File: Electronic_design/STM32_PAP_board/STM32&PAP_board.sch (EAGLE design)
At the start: 22 parts

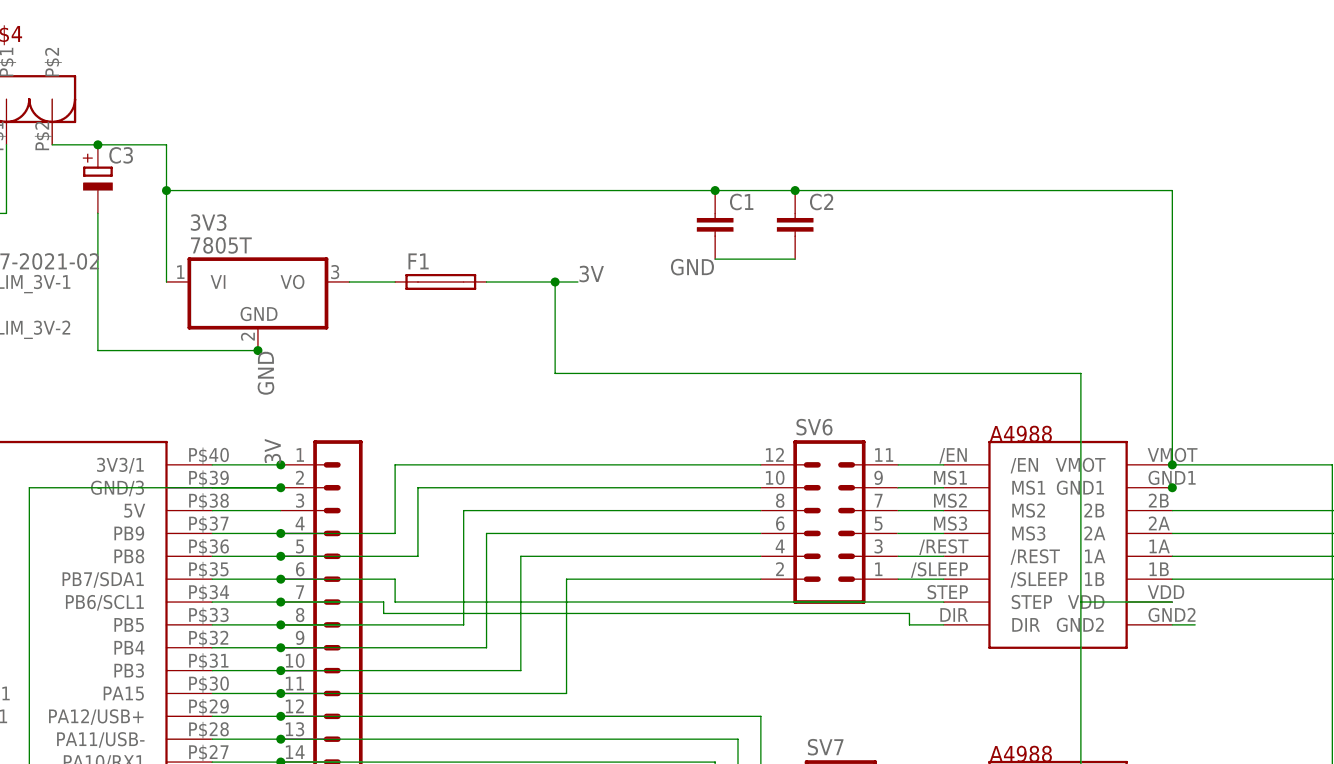
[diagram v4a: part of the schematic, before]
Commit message: modif sens connecteurs puissance
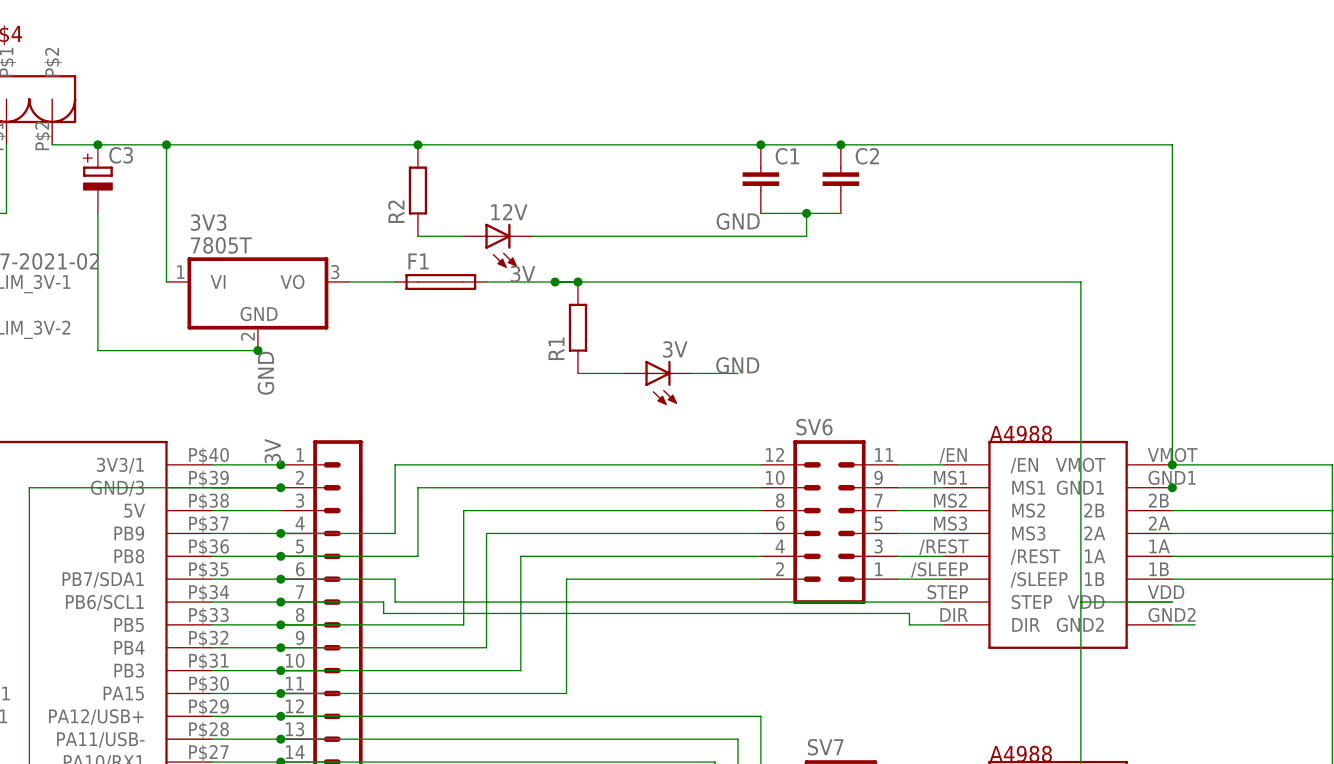
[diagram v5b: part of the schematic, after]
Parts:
- added 12V, 3V: (no value), eagle-ltspice:LED_ELD260
- added R1, R2: (no value), eagle-ltspice:R0204/7
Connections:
- new net N$43: 3V.A, R1.1
- new net N$47: 12V.A, R2.1
- net 3V: now also R1.2
- net GND: now also 12V.C, 3V.C
- net N$42: now also R2.2
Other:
- moved on the sheet: C1, C2
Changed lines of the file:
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@@
 <part name="SV2" library="con-lstb" library_urn="urn:adsk.eagle:library:162" deviceset="MA08-1" device="" package3d_urn="urn:adsk.eagle:package:8343/1"/>
 <part name="C3" library="rcl" library_urn="urn:adsk.eagle:library:334" deviceset="CPOL-EU" device="E5-13" package3d_urn="urn:adsk.eagle:package:23375/1"/>
+<part name="R1" library="eagle-ltspice" library_urn="urn:adsk.eagle:library:217" deviceset="R" device="0204/7" package3d_urn="urn:adsk.eagle:package:13274/1"/>
+<part name="3V" library="eagle-ltspice" library_urn="urn:adsk.eagle:library:217" deviceset="LED_E" device="LD260" package3d_urn="urn:adsk.eagle:package:13313/1"/>
+<part name="R2" library="eagle-ltspice" library_urn="urn:adsk.eagle:library:217" deviceset="R" device="0204/7" package3d_urn="urn:adsk.eagle:package:13274/1"/>
+<part name="12V" library="eagle-ltspice" library_urn="urn:adsk.eagle:library:217" deviceset="LED_E" device="LD260" package3d_urn="urn:adsk.eagle:package:13313/1"/>
 </parts>
 <sheets>
@@
 <instance part="SV10" gate="G$1" x="-106.68" y="-53.34"/>
 <instance part="SV11" gate="G$1" x="-125.73" y="-54.61"/>
-<instance part="C1" gate="G$1" x="35.56" y="58.42"/>
-<instance part="C2" gate="G$1" x="44.45" y="58.42"/>
+<instance part="C1" gate="G$1" x="40.64" y="63.5"/>
+<instance part="C2" gate="G$1" x="49.53" y="63.5"/>
 <instance part="F1" gate="1" x="5.08" y="50.8"/>
 <instance part="UART2" gate="G$1" x="-106.68" y="15.24"/>
@@
 <instance part="SV2" gate="1" x="-93.98" y="-5.08"/>
 <instance part="C3" gate="G$1" x="-33.02" y="63.5"/>
+<instance part="R1" gate="G$1" x="20.32" y="45.72" rot="R90"/>
+<instance part="3V" gate="G$1" x="27.94" y="40.64" rot="R90"/>
+<instance part="R2" gate="G$1" x="2.54" y="60.96" rot="R90"/>
+<instance part="12V" gate="G$1" x="10.16" y="55.88" rot="R90"/>
 </instances>
 <busses>
@@
 <pinref part="C1" gate="G$1" pin="2"/>
 <pinref part="C2" gate="G$1" pin="2"/>
-<wire x1="35.56" y1="53.34" x2="44.45" y2="53.34" width="0.1524" layer="91"/>
-<label x="35.56" y="53.34" size="1.778" layer="95" rot="R180"/>
+<wire x1="40.64" y1="58.42" x2="45.72" y2="58.42" width="0.1524" layer="91"/>
+<label x="40.64" y="58.42" size="1.778" layer="95" rot="R180"/>
+<pinref part="12V" gate="G$1" pin="C"/>
+<wire x1="45.72" y1="58.42" x2="49.53" y2="58.42" width="0.1524" layer="91"/>
+<wire x1="15.24" y1="55.88" x2="45.72" y2="55.88" width="0.1524" layer="91"/>
+<wire x1="45.72" y1="55.88" x2="45.72" y2="58.42" width="0.1524" layer="91"/>
+<junction x="45.72" y="58.42"/>
 </segment>
 <segment>
@@
 <label x="-99.06" y="22.86" size="1.778" layer="95"/>
 </segment>
+<segment>
+<pinref part="3V" gate="G$1" pin="C"/>
+<wire x1="33.02" y1="40.64" x2="38.1" y2="40.64" width="0.1524" layer="91"/>
+<label x="35.56" y="40.64" size="1.778" layer="95"/>
+</segment>
 </net>
 <net name="N$45" class="0">
@@
 <segment>
 <pinref part="3V3" gate="A1" pin="VI"/>
-<wire x1="-25.4" y1="50.8" x2="-25.4" y2="60.96" width="0.1524" layer="91"/>
+<wire x1="-25.4" y1="50.8" x2="-25.4" y2="66.04" width="0.1524" layer="91"/>
 <pinref part="U$1" gate="G$1" pin="VMOT"/>
-<wire x1="35.56" y1="60.96" x2="44.45" y2="60.96" width="0.1524" layer="91"/>
-<wire x1="44.45" y1="60.96" x2="86.36" y2="60.96" width="0.1524" layer="91"/>
-<wire x1="86.36" y1="60.96" x2="86.36" y2="30.48" width="0.1524" layer="91"/>
+<wire x1="40.64" y1="66.04" x2="49.53" y2="66.04" width="0.1524" layer="91"/>
+<wire x1="49.53" y1="66.04" x2="86.36" y2="66.04" width="0.1524" layer="91"/>
+<wire x1="86.36" y1="66.04" x2="86.36" y2="30.48" width="0.1524" layer="91"/>
 <pinref part="U$2" gate="G$1" pin="VMOT"/>
 <wire x1="86.36" y1="-5.08" x2="104.14" y2="-5.08" width="0.1524" layer="91"/>
@@
 <junction x="86.36" y="30.48"/>
 <pinref part="C1" gate="G$1" pin="1"/>
-<junction x="35.56" y="60.96"/>
+<junction x="40.64" y="66.04"/>
 <pinref part="C2" gate="G$1" pin="1"/>
-<junction x="44.45" y="60.96"/>
-<wire x1="-25.4" y1="60.96" x2="35.56" y2="60.96" width="0.1524" layer="91"/>
+<junction x="49.53" y="66.04"/>
+<wire x1="-25.4" y1="66.04" x2="2.54" y2="66.04" width="0.1524" layer="91"/>
 <pinref part="U$4" gate="G$1" pin="P$2"/>
+<wire x1="2.54" y1="66.04" x2="40.64" y2="66.04" width="0.1524" layer="91"/>
 <wire x1="-38.1" y1="66.04" x2="-33.02" y2="66.04" width="0.1524" layer="91"/>
 <wire x1="-33.02" y1="66.04" x2="-25.4" y2="66.04" width="0.1524" layer="91"/>
-<wire x1="-25.4" y1="66.04" x2="-25.4" y2="60.96" width="0.1524" layer="91"/>
-<junction x="-25.4" y="60.96"/>
+<junction x="-25.4" y="66.04"/>
 <pinref part="C3" gate="G$1" pin="+"/>
 <junction x="-33.02" y="66.04"/>
+<pinref part="R2" gate="G$1" pin="2"/>
+<junction x="2.54" y="66.04"/>
 </segment>
 </net>
@@
 <net name="3V" class="0">
 <segment>
-<label x="20.32" y="50.8" size="1.778" layer="95"/>
+<label x="12.7" y="50.8" size="1.778" layer="95"/>
 <wire x1="20.32" y1="50.8" x2="17.78" y2="50.8" width="0.1524" layer="91"/>
-<wire x1="17.78" y1="50.8" x2="17.78" y2="40.64" width="0.1524" layer="91"/>
-<wire x1="17.78" y1="40.64" x2="76.2" y2="40.64" width="0.1524" layer="91"/>
+<wire x1="17.78" y1="50.8" x2="20.32" y2="50.8" width="0.1524" layer="91"/>
 <pinref part="U$2" gate="G$1" pin="VDD"/>
 <pinref part="U$1" gate="G$1" pin="VDD"/>
+<wire x1="20.32" y1="50.8" x2="76.2" y2="50.8" width="0.1524" layer="91"/>
 <wire x1="76.2" y1="15.24" x2="76.2" y2="-20.32" width="0.1524" layer="91"/>
 <wire x1="76.2" y1="-20.32" x2="86.36" y2="-20.32" width="0.1524" layer="91"/>
-<wire x1="76.2" y1="40.64" x2="76.2" y2="15.24" width="0.1524" layer="91"/>
+<wire x1="76.2" y1="50.8" x2="76.2" y2="15.24" width="0.1524" layer="91"/>
 <wire x1="76.2" y1="15.24" x2="86.36" y2="15.24" width="0.1524" layer="91"/>
 <pinref part="F1" gate="1" pin="2"/>
 <wire x1="10.16" y1="50.8" x2="17.78" y2="50.8" width="0.1524" layer="91"/>
 <junction x="17.78" y="50.8"/>
+<pinref part="R1" gate="G$1" pin="2"/>
+<junction x="20.32" y="50.8"/>
 </segment>
 <segment>
@@
 </segment>
 </net>
+<net name="N$43" class="0">
+<segment>
+<pinref part="R1" gate="G$1" pin="1"/>
+<pinref part="3V" gate="G$1" pin="A"/>
+<wire x1="20.32" y1="40.64" x2="25.4" y2="40.64" width="0.1524" layer="91"/>
+</segment>
+</net>
+<net name="N$47" class="0">
+<segment>
+<pinref part="R2" gate="G$1" pin="1"/>
+<pinref part="12V" gate="G$1" pin="A"/>
+<wire x1="2.54" y1="55.88" x2="7.62" y2="55.88" width="0.1524" layer="91"/>
+</segment>
+</net>
